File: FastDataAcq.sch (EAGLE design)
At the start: 215 parts, among them J1 MICRO-FIT_3.0_2POS_RA_SMD, J2 USB_MICROAB_SMT, U1 ADC08D500, U10 TMP421, U11 DAC101C081, U12 ADCMP553BRMZ, U13 XCFXXS04, U14 FT230XQ, U2 XC6SLX9-3TQG144C, U3 LTC2955-1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

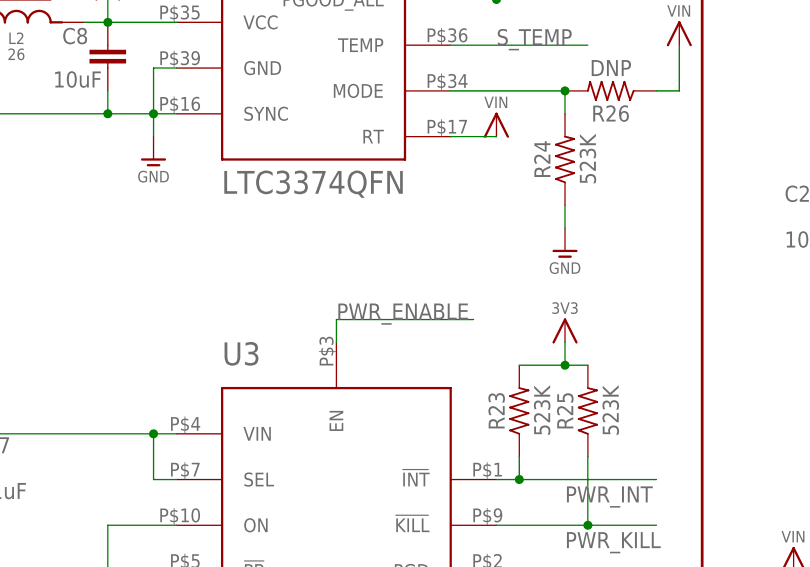
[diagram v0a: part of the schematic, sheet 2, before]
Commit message: FDA v0.9 Ready For Quote Submission
All that is left is shielding mounting holes.
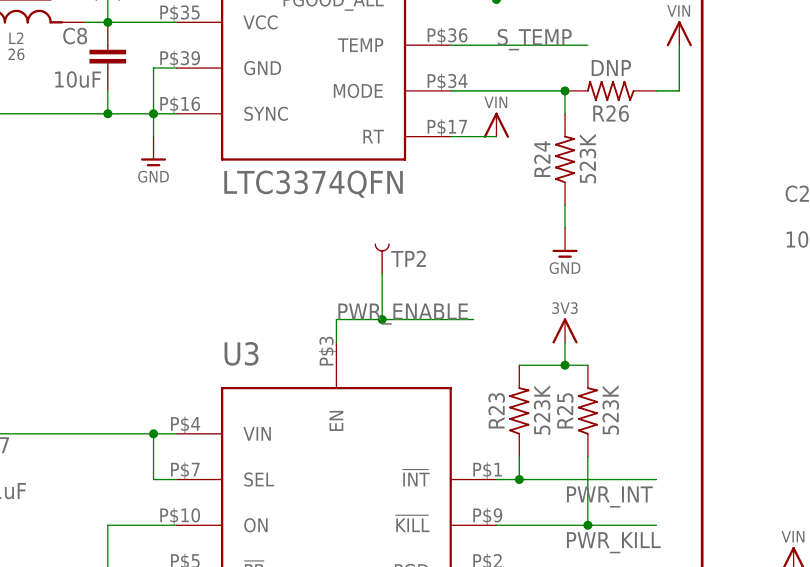
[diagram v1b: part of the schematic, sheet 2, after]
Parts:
- added TP1, TP2: TEST-POINT3, SparkFun-Passives:TEST-POINT3
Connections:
- net PWR_ENABLE: now also TP2.1
- net TRIG_REF: now also TP1.1
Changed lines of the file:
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@@
 <part name="U$94" library="Schuyler" deviceset="SUP_1V9A" device=""/>
 <part name="X3" library="Schuyler" deviceset="HEADER_0.1&quot;_8P_" device="2R_SMT"/>
+<part name="TP1" library="SparkFun-Passives" deviceset="TEST-POINT" device="3"/>
+<part name="TP2" library="SparkFun-Passives" deviceset="TEST-POINT" device="3"/>
 </parts>
 <sheets>
@@
 <attribute name="SUPPLIER" x="251.46" y="205.74" size="1.778" layer="96" rot="R270" display="off"/>
 </instance>
+<instance part="TP2" gate="G$1" x="96.52" y="205.74" smashed="yes" rot="R90">
+<attribute name="NAME" x="101.6" y="208.28" size="1.778" layer="95" rot="R180"/>
+</instance>
 </instances>
 <busses>
@@
 <pinref part="U3" gate="G$1" pin="EN"/>
 <wire x1="91.44" y1="198.12" x2="91.44" y2="200.66" width="0.1524" layer="91"/>
-<wire x1="91.44" y1="200.66" x2="106.68" y2="200.66" width="0.1524" layer="91"/>
+<wire x1="91.44" y1="200.66" x2="96.52" y2="200.66" width="0.1524" layer="91"/>
 <label x="91.44" y="200.66" size="1.778" layer="95"/>
+<pinref part="TP2" gate="G$1" pin="1"/>
+<wire x1="96.52" y1="200.66" x2="106.68" y2="200.66" width="0.1524" layer="91"/>
+<wire x1="96.52" y1="205.74" x2="96.52" y2="200.66" width="0.1524" layer="91"/>
+<junction x="96.52" y="200.66"/>
 </segment>
 </net>
@@
 <instance part="U$3" gate="G$1" x="355.6" y="83.82"/>
 <instance part="X3" gate="G$1" x="182.88" y="134.62" rot="R90"/>
+<instance part="TP1" gate="G$1" x="177.8" y="101.6" rot="R90"/>
 </instances>
 <busses>
@@
 <label x="162.56" y="96.52" size="1.778" layer="95"/>
 <wire x1="177.8" y1="96.52" x2="160.02" y2="96.52" width="0.1524" layer="91"/>
-<wire x1="177.8" y1="99.06" x2="177.8" y2="96.52" width="0.1524" layer="91"/>
 <junction x="177.8" y="96.52"/>
+<pinref part="TP1" gate="G$1" pin="1"/>
+<wire x1="177.8" y1="96.52" x2="177.8" y2="101.6" width="0.1524" layer="91"/>
 </segment>
 <segment>

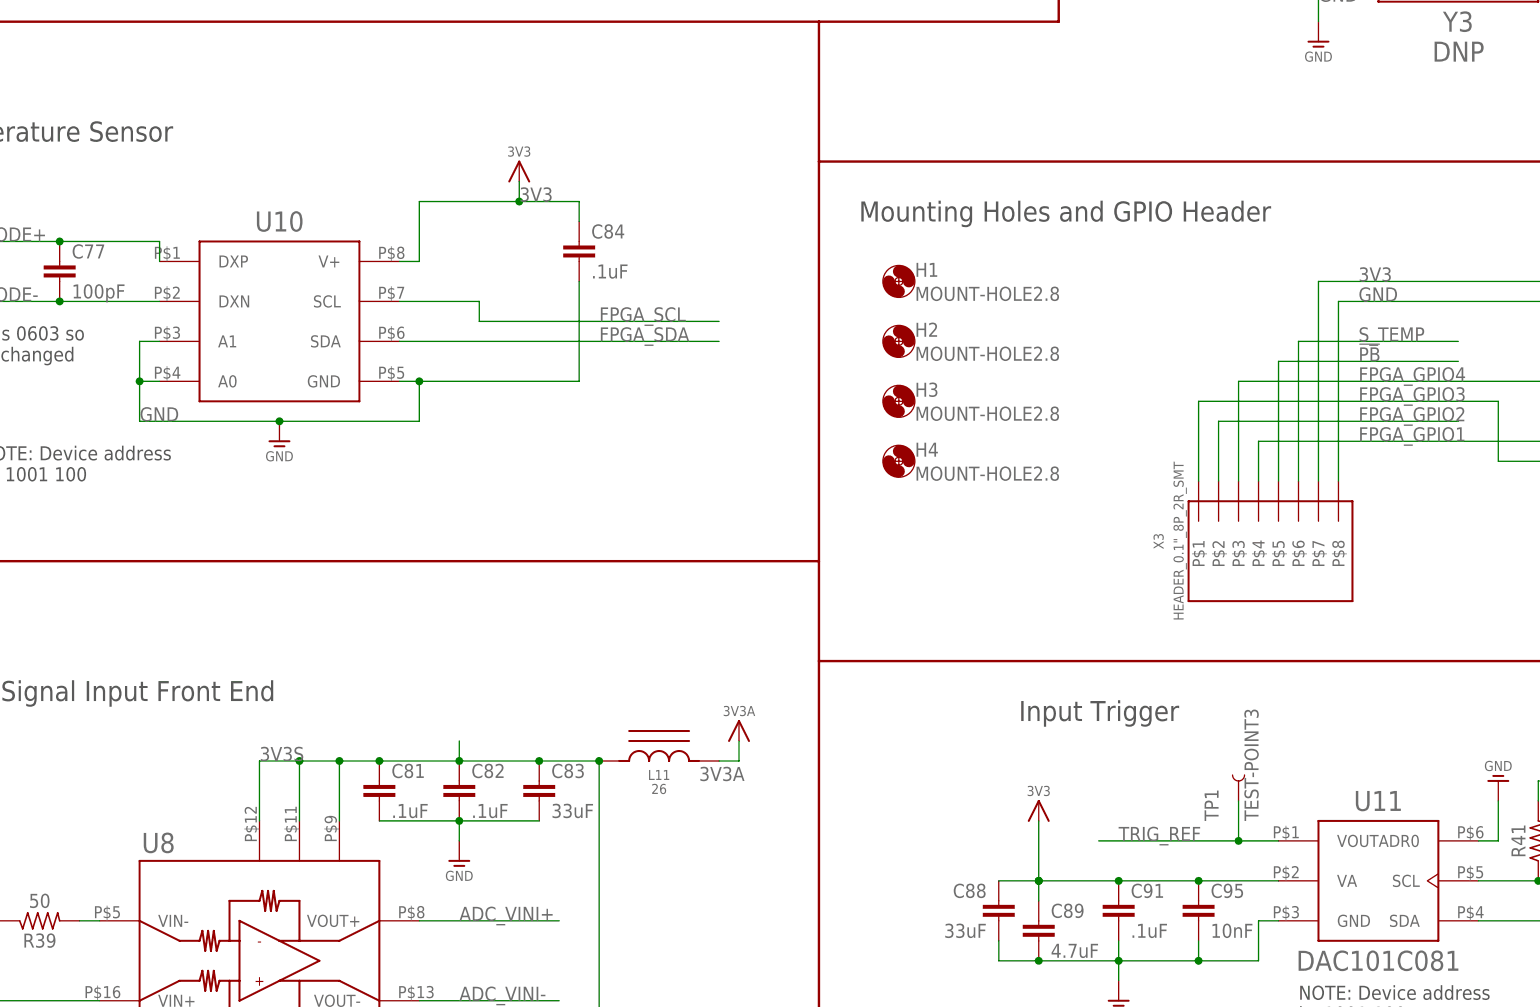
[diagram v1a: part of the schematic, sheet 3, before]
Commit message: Minor Changes - Fixed Screw Holes
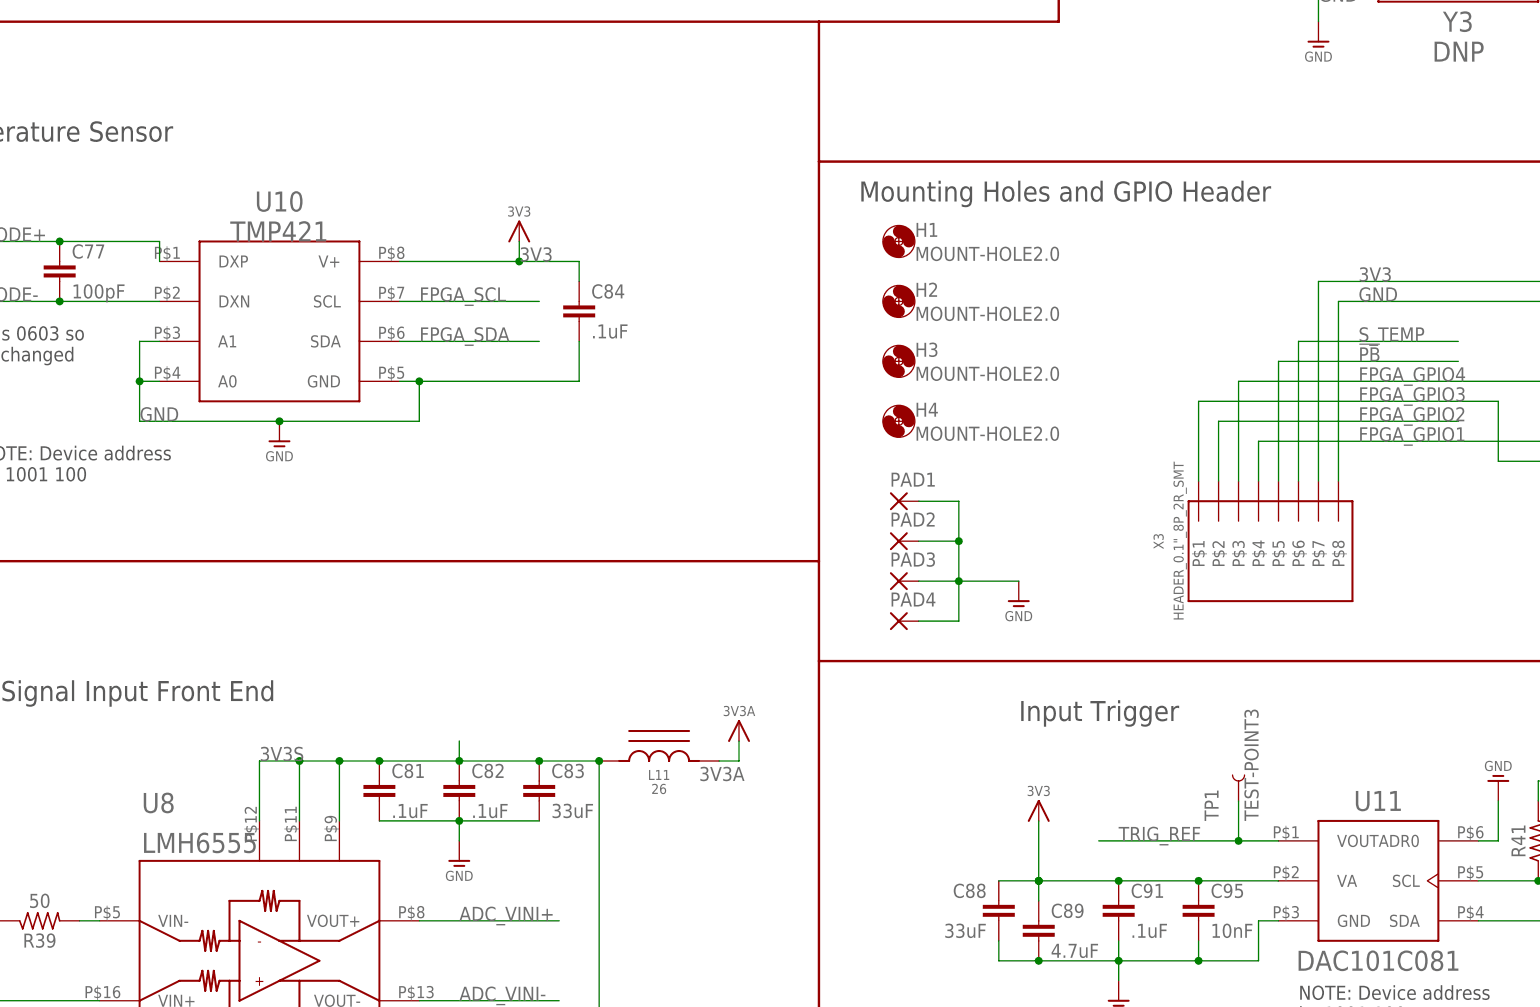
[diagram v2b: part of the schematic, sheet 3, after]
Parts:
- added PAD1, PAD2, PAD3, PAD4: (no value), wirepad:SMD2
- H1, H2, H3, H4: value MOUNT-HOLE2.8 -> MOUNT-HOLE2.0; device holes:MOUNT-HOLE2.8 -> holes:MOUNT-HOLE2.0
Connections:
- net GND: now also PAD1.P, PAD2.P, PAD3.P, PAD4.P
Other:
- moved on the sheet: C84, H1, H2, H3, H4
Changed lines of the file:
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@@
 <attribute name="SUPPLIER" value="DIGIKEY"/>
 </part>
-<part name="H1" library="holes" deviceset="MOUNT-HOLE" device="2.8"/>
-<part name="H2" library="holes" deviceset="MOUNT-HOLE" device="2.8"/>
-<part name="H3" library="holes" deviceset="MOUNT-HOLE" device="2.8"/>
-<part name="H4" library="holes" deviceset="MOUNT-HOLE" device="2.8"/>
+<part name="H1" library="holes" deviceset="MOUNT-HOLE" device="2.0" value="MOUNT-HOLE2.0"/>
+<part name="H2" library="holes" deviceset="MOUNT-HOLE" device="2.0" value="MOUNT-HOLE2.0"/>
+<part name="H3" library="holes" deviceset="MOUNT-HOLE" device="2.0" value="MOUNT-HOLE2.0"/>
+<part name="H4" library="holes" deviceset="MOUNT-HOLE" device="2.0" value="MOUNT-HOLE2.0"/>
 <part name="D1" library="Schuyler" deviceset="LED_" device="0603_RED">
 <attribute name="MANPARTNUMBER" value=""/>
@@
 <part name="TP1" library="SparkFun-Passives" deviceset="TEST-POINT" device="3"/>
 <part name="TP2" library="SparkFun-Passives" deviceset="TEST-POINT" device="3"/>
+<part name="PAD2" library="wirepad" deviceset="SMD2" device=""/>
+<part name="PAD1" library="wirepad" deviceset="SMD2" device=""/>
+<part name="PAD3" library="wirepad" deviceset="SMD2" device=""/>
+<part name="PAD4" library="wirepad" deviceset="SMD2" device=""/>
+<part name="U$1" library="Schuyler" deviceset="SUP_GND" device=""/>
 </parts>
 <sheets>
@@
 <text x="327.66" y="27.94" size="3.81" layer="94">Additional Support ICs</text>
 <wire x1="124.46" y1="182.88" x2="259.08" y2="182.88" width="0.3048" layer="94"/>
-<text x="129.54" y="175.26" size="2.54" layer="97" font="vector">Mounting Holes and GPIO Header</text>
+<text x="129.54" y="177.8" size="2.54" layer="97" font="vector">Mounting Holes and GPIO Header</text>
 <text x="229.362" y="157.226" size="1.778" layer="96">Blue</text>
 <text x="239.522" y="157.48" size="1.778" layer="96">Green</text>
@@
 <instance part="C97" gate="G$1" x="238.76" y="208.28"/>
 <instance part="U10" gate="G$1" x="55.88" y="162.56"/>
-<instance part="C84" gate="G$1" x="93.98" y="172.72"/>
-<instance part="SUPPLY44" gate="G$1" x="86.36" y="180.34"/>
+<instance part="C84" gate="G$1" x="93.98" y="165.1"/>
+<instance part="SUPPLY44" gate="G$1" x="86.36" y="172.72"/>
 <instance part="C77" gate="G$1" x="27.94" y="170.18">
 <attribute name="PARTNUMBER" x="27.94" y="170.18" size="1.778" layer="96" display="off"/>
@@
 </instance>
 <instance part="L13" gate="G$1" x="332.74" y="81.28" rot="R90"/>
-<instance part="H1" gate="G$1" x="134.62" y="167.64"/>
-<instance part="H2" gate="G$1" x="134.62" y="160.02"/>
-<instance part="H3" gate="G$1" x="134.62" y="152.4"/>
-<instance part="H4" gate="G$1" x="134.62" y="144.78"/>
+<instance part="H1" gate="G$1" x="134.62" y="172.72"/>
+<instance part="H2" gate="G$1" x="134.62" y="165.1"/>
+<instance part="H3" gate="G$1" x="134.62" y="157.48"/>
+<instance part="H4" gate="G$1" x="134.62" y="149.86"/>
 <instance part="D5" gate="G$1" x="396.24" y="106.68"/>
 <instance part="D6" gate="G$1" x="411.48" y="106.68"/>
@@
 <instance part="X3" gate="G$1" x="182.88" y="134.62" rot="R90"/>
 <instance part="TP1" gate="G$1" x="177.8" y="101.6" rot="R90"/>
+<instance part="PAD2" gate="1" x="134.62" y="134.62"/>
+<instance part="PAD1" gate="1" x="134.62" y="139.7"/>
+<instance part="PAD3" gate="1" x="134.62" y="129.54"/>
+<instance part="PAD4" gate="1" x="134.62" y="124.46"/>
+<instance part="U$1" gate="G$1" x="149.86" y="129.54"/>
 </instances>
 <busses>
@@
 <segment>
 <pinref part="SUPPLY44" gate="G$1" pin="3V3"/>
-<wire x1="86.36" y1="180.34" x2="86.36" y2="177.8" width="0.1524" layer="91"/>
-<label x="86.36" y="177.8" size="1.778" layer="95"/>
+<wire x1="86.36" y1="172.72" x2="86.36" y2="170.18" width="0.1524" layer="91"/>
+<label x="86.36" y="170.18" size="1.778" layer="95"/>
 <pinref part="U10" gate="G$1" pin="V+"/>
-<wire x1="71.12" y1="170.18" x2="73.66" y2="170.18" width="0.1524" layer="91"/>
-<wire x1="73.66" y1="170.18" x2="73.66" y2="177.8" width="0.1524" layer="91"/>
-<wire x1="73.66" y1="177.8" x2="86.36" y2="177.8" width="0.1524" layer="91"/>
-<wire x1="86.36" y1="177.8" x2="93.98" y2="177.8" width="0.1524" layer="91"/>
-<junction x="86.36" y="177.8"/>
+<wire x1="71.12" y1="170.18" x2="86.36" y2="170.18" width="0.1524" layer="91"/>
+<wire x1="86.36" y1="170.18" x2="93.98" y2="170.18" width="0.1524" layer="91"/>
+<junction x="86.36" y="170.18"/>
 <pinref part="C84" gate="G$1" pin="1"/>
-<wire x1="93.98" y1="175.26" x2="93.98" y2="177.8" width="0.1524" layer="91"/>
+<wire x1="93.98" y1="167.64" x2="93.98" y2="170.18" width="0.1524" layer="91"/>
 </segment>
 <segment>
@@
 <segment>
 <pinref part="U10" gate="G$1" pin="SCL"/>
-<wire x1="71.12" y1="165.1" x2="81.28" y2="165.1" width="0.1524" layer="91"/>
-<wire x1="81.28" y1="165.1" x2="81.28" y2="162.56" width="0.1524" layer="91"/>
-<wire x1="81.28" y1="162.56" x2="111.76" y2="162.56" width="0.1524" layer="91"/>
-<label x="96.52" y="162.56" size="1.778" layer="95"/>
+<wire x1="71.12" y1="165.1" x2="88.9" y2="165.1" width="0.1524" layer="91"/>
+<label x="73.66" y="165.1" size="1.778" layer="95"/>
 </segment>
 <segment>
@@
 <segment>
 <pinref part="U10" gate="G$1" pin="SDA"/>
-<wire x1="71.12" y1="160.02" x2="111.76" y2="160.02" width="0.1524" layer="91"/>
-<label x="96.52" y="160.02" size="1.778" layer="95"/>
+<wire x1="71.12" y1="160.02" x2="88.9" y2="160.02" width="0.1524" layer="91"/>
+<label x="73.66" y="160.02" size="1.778" layer="95"/>
 </segment>
 <segment>
@@
 <wire x1="55.88" y1="149.86" x2="38.1" y2="149.86" width="0.1524" layer="91"/>
 <wire x1="73.66" y1="154.94" x2="93.98" y2="154.94" width="0.1524" layer="91"/>
-<wire x1="93.98" y1="154.94" x2="93.98" y2="167.64" width="0.1524" layer="91"/>
+<wire x1="93.98" y1="154.94" x2="93.98" y2="160.02" width="0.1524" layer="91"/>
 <junction x="73.66" y="154.94"/>
 <label x="38.1" y="149.86" size="1.778" layer="95"/>
@@
 <pinref part="U$3" gate="G$1" pin="GND"/>
 </segment>
+<segment>
+<pinref part="PAD4" gate="1" pin="P"/>
+<wire x1="137.16" y1="124.46" x2="142.24" y2="124.46" width="0.1524" layer="91"/>
+<wire x1="142.24" y1="124.46" x2="142.24" y2="129.54" width="0.1524" layer="91"/>
+<pinref part="PAD3" gate="1" pin="P"/>
+<wire x1="137.16" y1="129.54" x2="142.24" y2="129.54" width="0.1524" layer="91"/>
+<pinref part="U$1" gate="G$1" pin="GND"/>
+<wire x1="142.24" y1="129.54" x2="149.86" y2="129.54" width="0.1524" layer="91"/>
+<junction x="142.24" y="129.54"/>
+<pinref part="PAD2" gate="1" pin="P"/>
+<wire x1="137.16" y1="134.62" x2="142.24" y2="134.62" width="0.1524" layer="91"/>
+<wire x1="142.24" y1="134.62" x2="142.24" y2="129.54" width="0.1524" layer="91"/>
+<pinref part="PAD1" gate="1" pin="P"/>
+<wire x1="137.16" y1="139.7" x2="142.24" y2="139.7" width="0.1524" layer="91"/>
+<wire x1="142.24" y1="139.7" x2="142.24" y2="134.62" width="0.1524" layer="91"/>
+<junction x="142.24" y="134.62"/>
+</segment>
 </net>

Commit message: Fixed consistency issue between sch and brd
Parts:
- X4: PARTNUMBER 57J0374 -> (none); SUPPLIER Newark -> (none)
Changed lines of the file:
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@@
 <attribute name="SUPPLIER" value="DIGIKEY"/>
 </part>
-<part name="X4" library="con-molex" deviceset="87832-14" device="">
-<attribute name="PARTNUMBER" value="57J0374"/>
-<attribute name="SUPPLIER" value="Newark"/>
-</part>
+<part name="X4" library="con-molex" deviceset="87832-14" device=""/>
 <part name="SUPPLY29" library="Schuyler" deviceset="SUP_3V3" device="" value="3V3"/>
 <part name="R7" library="rcl" deviceset="R-US_" device="R0603" value="3.3k 0.1%">

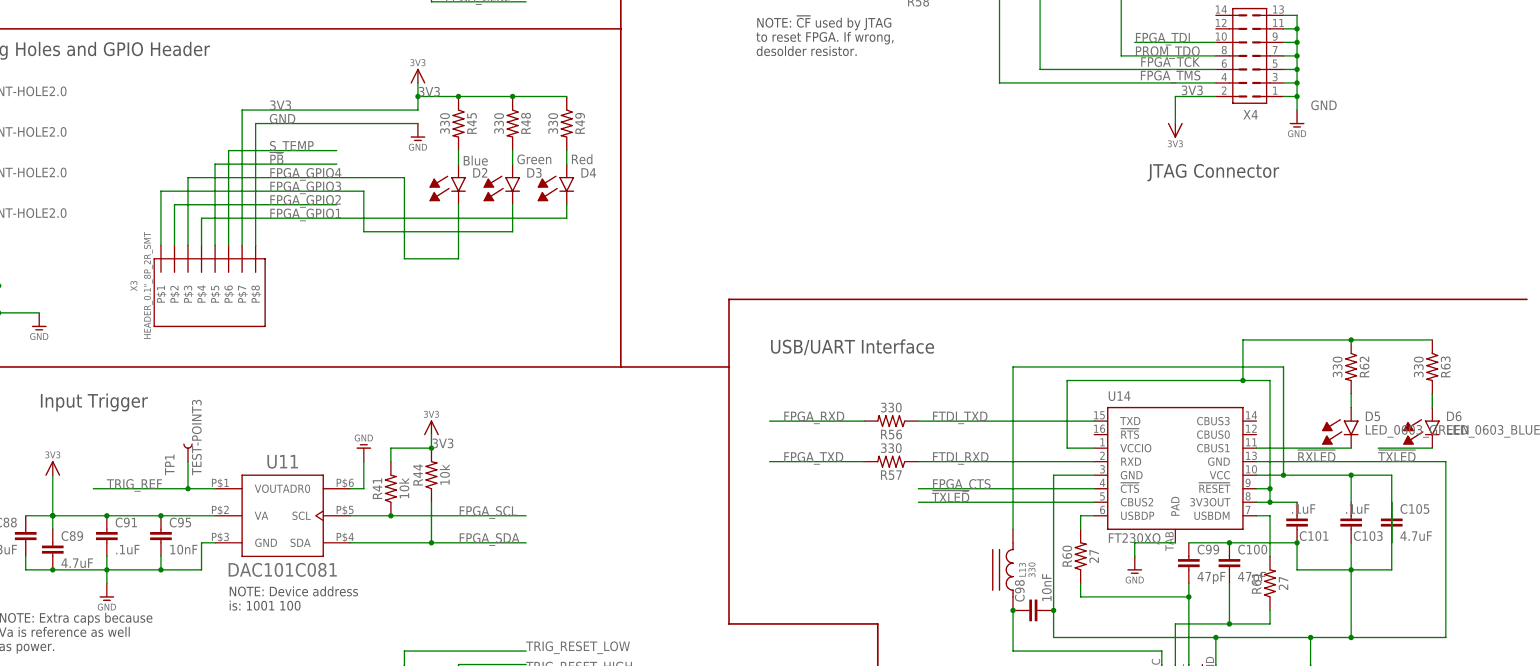
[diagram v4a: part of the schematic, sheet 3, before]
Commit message: Done with adjusting most of the LVDS track widths.
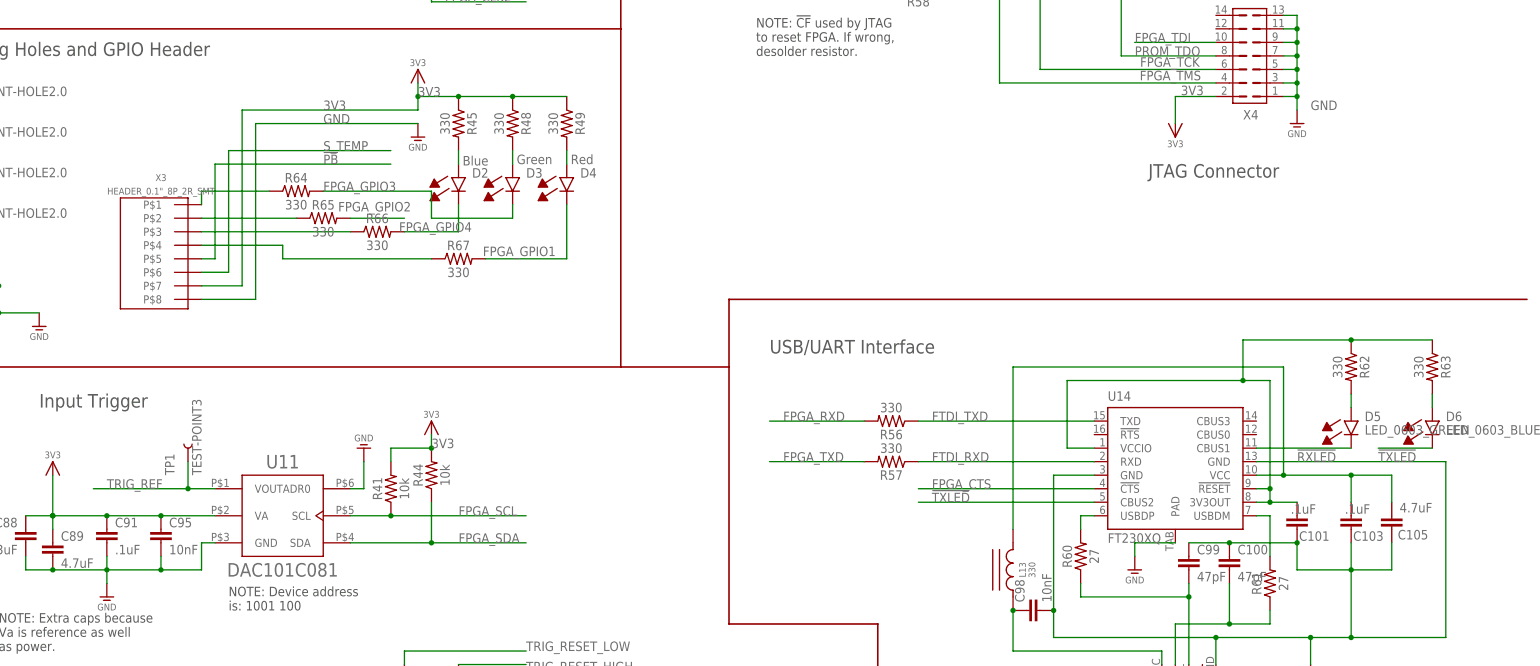
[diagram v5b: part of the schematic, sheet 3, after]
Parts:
- added R64, R65, R66, R67: 330, rcl:R-US_R0201
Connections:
- new net N$23: R65.1, X3.P$2
- new net N$25: R66.1, X3.P$3
- new net N$26: R67.1, X3.P$4
- new net N$9: R64.1, X3.P$1
- net FPGA_GPIO1: now also R67.2; no longer X3.P$4
- net FPGA_GPIO2: now also R65.2; no longer X3.P$2
- net FPGA_GPIO3: now also R64.2; no longer X3.P$1
- net FPGA_GPIO4: now also R66.2; no longer X3.P$3
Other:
- moved on the sheet: C105, X3
